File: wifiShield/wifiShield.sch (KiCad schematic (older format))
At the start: 19 parts, among them J1 USB_OTG, J2 CONN_02X06, J3 CONN_01X13, J4 CONN_01X05, J7 CONN_01X08, SW1 SW_Push, SW2 SW_Push, U2 FT232RL, U3 esp8266mod

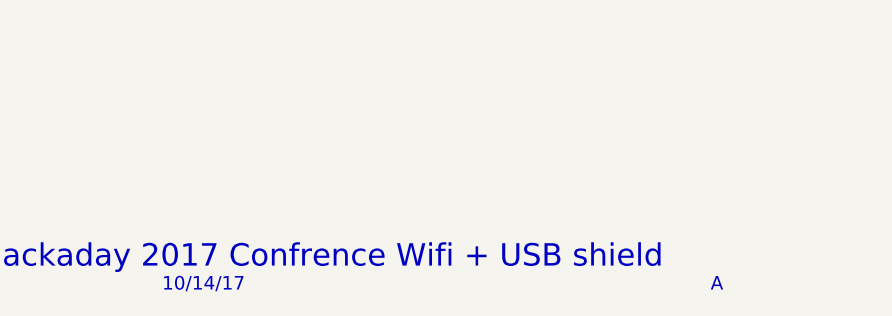
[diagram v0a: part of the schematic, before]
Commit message: Remove extra via and add REV to board
Board Rev bumped to Rev B
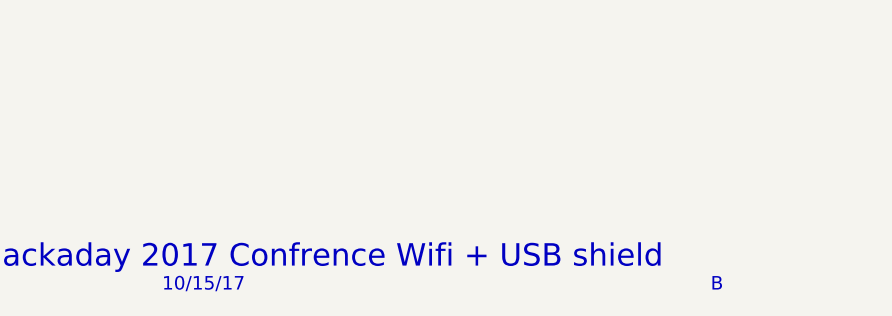
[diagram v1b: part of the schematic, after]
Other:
- note added: "10/15/17"
- note added: "B"
- note removed: "10/14/17"
- note removed: "A"
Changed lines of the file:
@@
 Hackaday 2017 Confrence Wifi + USB shield\n
 Text Notes 8150 7650 0    59   ~ 0
-10/14/17
+10/15/17
 Text Notes 10550 7650 0    59   ~ 0
-A
+B
 $EndSCHEMATC
